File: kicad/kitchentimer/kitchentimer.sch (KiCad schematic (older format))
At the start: 34 parts, among them J1 CONN_01X06, SW1 SWITCH, SW2 SWITCH, SW3 SWITCH, SW4 SWITCH, SW5 SWITCH, SW6 SWITCH, SW7 SWITCH, U1 74HC595, U2 74HC595, U3 74LS165, U4 74HC595, U5 74HC595

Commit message: Associate components
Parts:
- AFF1, AFF2: footprint (none) -> Displays_7-Segment:7SegmentLED_LTS6760_LTS6780
- D1, D2, D3, D4, D5, D6: footprint (none) -> LEDs:LED_0805
- J1: footprint (none) -> Pin_Headers:Pin_Header_Straight_1x06
- R1, R10, R11, R12, R13, R2, R3, R4, R5, R6, R7, R8, R9: footprint (none) -> Resistors_SMD:R_0805_HandSoldering
- SW1, SW2, SW3, SW4, SW5, SW6, SW7: footprint (none) -> Buttons_Switches_THT:SW_PUSH_6mm
- U1, U2, U3, U4, U5: footprint (none) -> Housings_DIP:DIP-16_W7.62mm
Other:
- note added: "LATCH SWITCH"
- note removed: "LATCH 165"
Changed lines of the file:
@@
 F 0 "U5" V 8850 1000 50  0000 L CNN
 F 1 "74HC595" V 8850 1500 50  0000 L CNN
-F 2 "" H 3850 -1800 50  0001 C CNN
+F 2 "Housings_DIP:DIP-16_W7.62mm" H 3850 -1800 50  0001 C CNN
 F 3 "" H 3850 -1800 50  0001 C CNN
 	1    8850 1700
@@
 F 0 "U4" V 8750 2900 50  0000 L CNN
 F 1 "74HC595" V 8750 3400 50  0000 L CNN
-F 2 "" H 3750 100 50  0001 C CNN
+F 2 "Housings_DIP:DIP-16_W7.62mm" H 3750 100 50  0001 C CNN
 F 3 "" H 3750 100 50  0001 C CNN
 	1    8750 3600
@@
 F 0 "U1" V 3800 3700 50  0000 L CNN
 F 1 "74HC595" V 3800 4200 50  0000 L CNN
-F 2 "" H -1200 900 50  0001 C CNN
+F 2 "Housings_DIP:DIP-16_W7.62mm" H -1200 900 50  0001 C CNN
 F 3 "" H -1200 900 50  0001 C CNN
 	1    3800 4400
@@
 F 0 "U2" V 5700 1900 50  0000 L CNN
 F 1 "74HC595" V 5700 2450 50  0000 L CNN
-F 2 "" H 700 -850 50  0001 C CNN
+F 2 "Housings_DIP:DIP-16_W7.62mm" H 700 -850 50  0001 C CNN
 F 3 "" H 700 -850 50  0001 C CNN
 	1    5700 2650
@@
 F 0 "J1" V 5015 762 50  0000 R CNN
 F 1 "CONN_01X06" V 4924 762 50  0000 R CNN
-F 2 "" H -200 0   50  0001 C CNN
+F 2 "Pin_Headers:Pin_Header_Straight_1x06" H -200 0   50  0001 C CNN
 F 3 "" H -200 0   50  0001 C CNN
 	1    5050 1100
@@
 F 0 "U3" V 5800 5250 50  0000 R CNN
 F 1 "74LS165" V 5800 4600 50  0000 R CNN
-F 2 "" H 2750 3050 50  0001 C CNN
+F 2 "Housings_DIP:DIP-16_W7.62mm" H 2750 3050 50  0001 C CNN
 F 3 "" H 2750 3050 50  0001 C CNN
 	1    5800 4450
@@
 NoConn ~ 5200 5150
 NoConn ~ 5400 3750
-Text Notes 6700 4000 3    60   ~ 0
-LATCH 165
+Text Notes 6650 4550 1    60   ~ 0
+LATCH SWITCH
 $Comp
 L 7SEGMENTS AFF1
@@
 F 0 "AFF1" H 10500 2425 50  0000 C CNN
 F 1 "7SEGMENTS" H 10500 2334 50  0000 C CNN
-F 2 "" H 3350 -2800 50  0001 C CNN
+F 2 "Displays_7-Segment:7SegmentLED_LTS6760_LTS6780" H 3350 -2800 50  0001 C CNN
 F 3 "" H 3350 -2800 50  0001 C CNN
 	1    10500 1750
@@
 F 0 "AFF2" H 10550 4575 50  0000 C CNN
 F 1 "7SEGMENTS" H 10550 4484 50  0000 C CNN
-F 2 "" H 3400 -650 50  0001 C CNN
+F 2 "Displays_7-Segment:7SegmentLED_LTS6760_LTS6780" H 3400 -650 50  0001 C CNN
 F 3 "" H 3400 -650 50  0001 C CNN
 	1    10550 3900
@@
 F 0 "D6" V 2488 5933 50  0000 R CNN
 F 1 "LED" V 2397 5933 50  0000 R CNN
-F 2 "" H -1000 600 50  0001 C CNN
+F 2 "LEDs:LED_0805" H -1000 600 50  0001 C CNN
 F 3 "" H -1000 600 50  0001 C CNN
 	1    2450 6050
@@
 F 0 "R6" H 2380 5604 50  0000 R CNN
 F 1 "R" H 2380 5695 50  0000 R CNN
-F 2 "" V -920 0   50  0001 C CNN
+F 2 "Resistors_SMD:R_0805_HandSoldering" V -920 0   50  0001 C CNN
 F 3 "" H -850 0   50  0001 C CNN
 	1    2450 5650
@@
 F 0 "R5" H 2230 5604 50  0000 R CNN
 F 1 "R" H 2230 5695 50  0000 R CNN
-F 2 "" V -1070 0   50  0001 C CNN
+F 2 "Resistors_SMD:R_0805_HandSoldering" V -1070 0   50  0001 C CNN
 F 3 "" H -1000 0   50  0001 C CNN
 	1    2300 5650
@@
 F 0 "D5" V 2338 5933 50  0000 R CNN
 F 1 "LED" V 2247 5933 50  0000 R CNN
-F 2 "" H -1150 600 50  0001 C CNN
+F 2 "LEDs:LED_0805" H -1150 600 50  0001 C CNN
 F 3 "" H -1150 600 50  0001 C CNN
 	1    2300 6050
@@
 F 0 "R4" H 2080 5604 50  0000 R CNN
 F 1 "R" H 2080 5695 50  0000 R CNN
-F 2 "" V -1220 0   50  0001 C CNN
+F 2 "Resistors_SMD:R_0805_HandSoldering" V -1220 0   50  0001 C CNN
 F 3 "" H -1150 0   50  0001 C CNN
 	1    2150 5650
@@
 F 0 "D4" V 2188 5933 50  0000 R CNN
 F 1 "LED" V 2097 5933 50  0000 R CNN
-F 2 "" H -1300 600 50  0001 C CNN
+F 2 "LEDs:LED_0805" H -1300 600 50  0001 C CNN
 F 3 "" H -1300 600 50  0001 C CNN
 	1    2150 6050
@@
 F 0 "R3" H 1930 5604 50  0000 R CNN
 F 1 "R" H 1930 5695 50  0000 R CNN
-F 2 "" V -1370 0   50  0001 C CNN
+F 2 "Resistors_SMD:R_0805_HandSoldering" V -1370 0   50  0001 C CNN
 F 3 "" H -1300 0   50  0001 C CNN
 	1    2000 5650
@@
 F 0 "D3" V 2038 5933 50  0000 R CNN
 F 1 "LED" V 1947 5933 50  0000 R CNN
-F 2 "" H -1450 600 50  0001 C CNN
+F 2 "LEDs:LED_0805" H -1450 600 50  0001 C CNN
 F 3 "" H -1450 600 50  0001 C CNN
 	1    2000 6050
@@
 F 0 "D2" V 1888 5933 50  0000 R CNN
 F 1 "LED" V 1797 5933 50  0000 R CNN
-F 2 "" H -1600 600 50  0001 C CNN
+F 2 "LEDs:LED_0805" H -1600 600 50  0001 C CNN
 F 3 "" H -1600 600 50  0001 C CNN
 	1    1850 6050
@@
 F 0 "D1" V 1738 5933 50  0000 R CNN
 F 1 "LED" V 1647 5933 50  0000 R CNN
-F 2 "" H -1750 600 50  0001 C CNN
+F 2 "LEDs:LED_0805" H -1750 600 50  0001 C CNN
 F 3 "" H -1750 600 50  0001 C CNN
 	1    1700 6050
@@
 F 0 "R2" H 1780 5604 50  0000 R CNN
 F 1 "R" H 1780 5695 50  0000 R CNN
-F 2 "" V -1520 0   50  0001 C CNN
+F 2 "Resistors_SMD:R_0805_HandSoldering" V -1520 0   50  0001 C CNN
 F 3 "" H -1450 0   50  0001 C CNN
 	1    1850 5650
@@
 F 0 "R1" H 1630 5604 50  0000 R CNN
 F 1 "R" H 1630 5695 50  0000 R CNN
-F 2 "" V -1670 0   50  0001 C CNN
+F 2 "Resistors_SMD:R_0805_HandSoldering" V -1670 0   50  0001 C CNN
 F 3 "" H -1600 0   50  0001 C CNN
 	1    1700 5650
@@
 F 0 "SW1" V 4650 5850 60  0000 L CNN
 F 1 "SWITCH" H 5250 5900 60  0000 L CNN
-F 2 "" H 1550 3450 60  0000 C CNN
+F 2 "Buttons_Switches_THT:SW_PUSH_6mm" H 1550 3450 60  0001 C CNN
 F 3 "" H 1550 3450 60  0000 C CNN
 	1    4950 5900
@@
 F 0 "R7" H 5020 6696 50  0000 L CNN
 F 1 "R" H 5020 6605 50  0000 L CNN
-F 2 "" V 230 700 50  0001 C CNN
+F 2 "Resistors_SMD:R_0805_HandSoldering" V 230 700 50  0001 C CNN
 F 3 "" H 300 700 50  0001 C CNN
 	1    4950 6650
@@
 F 0 "R8" H 5170 6696 50  0000 L CNN
 F 1 "R" H 5170 6605 50  0000 L CNN
-F 2 "" V 380 700 50  0001 C CNN
+F 2 "Resistors_SMD:R_0805_HandSoldering" V 380 700 50  0001 C CNN
 F 3 "" H 450 700 50  0001 C CNN
 	1    5100 6650
@@
 F 0 "SW2" V 4800 5850 60  0000 L CNN
 F 1 "SWITCH" H 5400 5900 60  0000 L CNN
-F 2 "" H 1700 3450 60  0000 C CNN
+F 2 "Buttons_Switches_THT:SW_PUSH_6mm" H 1700 3450 60  0001 C CNN
 F 3 "" H 1700 3450 60  0000 C CNN
 	1    5100 5900
@@
 F 0 "SW3" V 4950 5850 60  0000 L CNN
 F 1 "SWITCH" H 5550 5900 60  0000 L CNN
-F 2 "" H 1850 3450 60  0000 C CNN
+F 2 "Buttons_Switches_THT:SW_PUSH_6mm" H 1850 3450 60  0001 C CNN
 F 3 "" H 1850 3450 60  0000 C CNN
 	1    5250 5900
@@
 F 0 "R9" H 5320 6696 50  0000 L CNN
 F 1 "R" H 5320 6605 50  0000 L CNN
-F 2 "" V 530 700 50  0001 C CNN
+F 2 "Resistors_SMD:R_0805_HandSoldering" V 530 700 50  0001 C CNN
 F 3 "" H 600 700 50  0001 C CNN
 	1    5250 6650
@@
 F 0 "R10" H 5470 6696 50  0000 L CNN
 F 1 "R" H 5470 6605 50  0000 L CNN
-F 2 "" V 680 700 50  0001 C CNN
+F 2 "Resistors_SMD:R_0805_HandSoldering" V 680 700 50  0001 C CNN
 F 3 "" H 750 700 50  0001 C CNN
 	1    5400 6650
@@
 F 0 "R11" H 5620 6696 50  0000 L CNN
 F 1 "R" H 5620 6605 50  0000 L CNN
-F 2 "" V 830 700 50  0001 C CNN
+F 2 "Resistors_SMD:R_0805_HandSoldering" V 830 700 50  0001 C CNN
 F 3 "" H 900 700 50  0001 C CNN
 	1    5550 6650
@@
 F 0 "R12" H 5770 6696 50  0000 L CNN
 F 1 "R" H 5770 6605 50  0000 L CNN
-F 2 "" V 980 700 50  0001 C CNN
+F 2 "Resistors_SMD:R_0805_HandSoldering" V 980 700 50  0001 C CNN
 F 3 "" H 1050 700 50  0001 C CNN
 	1    5700 6650
@@
 F 0 "R13" H 5920 6696 50  0000 L CNN
 F 1 "R" H 5920 6605 50  0000 L CNN
-F 2 "" V 1130 700 50  0001 C CNN
+F 2 "Resistors_SMD:R_0805_HandSoldering" V 1130 700 50  0001 C CNN
 F 3 "" H 1200 700 50  0001 C CNN
 	1    5850 6650
@@
 F 0 "SW4" V 5100 5850 60  0000 L CNN
 F 1 "SWITCH" H 5700 5900 60  0000 L CNN
-F 2 "" H 2000 3450 60  0000 C CNN
+F 2 "Buttons_Switches_THT:SW_PUSH_6mm" H 2000 3450 60  0001 C CNN
 F 3 "" H 2000 3450 60  0000 C CNN
 	1    5400 5900
@@
 F 0 "SW5" V 5250 5850 60  0000 L CNN
 F 1 "SWITCH" H 5850 5900 60  0000 L CNN
-F 2 "" H 2150 3450 60  0000 C CNN
+F 2 "Buttons_Switches_THT:SW_PUSH_6mm" H 2150 3450 60  0001 C CNN
 F 3 "" H 2150 3450 60  0000 C CNN
 	1    5550 5900
@@
 F 0 "SW6" V 5400 5850 60  0000 L CNN
 F 1 "SWITCH" H 6000 5900 60  0000 L CNN
-F 2 "" H 2300 3450 60  0000 C CNN
+F 2 "Buttons_Switches_THT:SW_PUSH_6mm" H 2300 3450 60  0001 C CNN
 F 3 "" H 2300 3450 60  0000 C CNN
 	1    5700 5900
@@
 F 0 "SW7" V 5550 5850 60  0000 L CNN
 F 1 "SWITCH" H 6150 5900 60  0000 L CNN
-F 2 "" H 2450 3450 60  0000 C CNN
+F 2 "Buttons_Switches_THT:SW_PUSH_6mm" H 2450 3450 60  0001 C CNN
 F 3 "" H 2450 3450 60  0000 C CNN
 	1    5850 5900

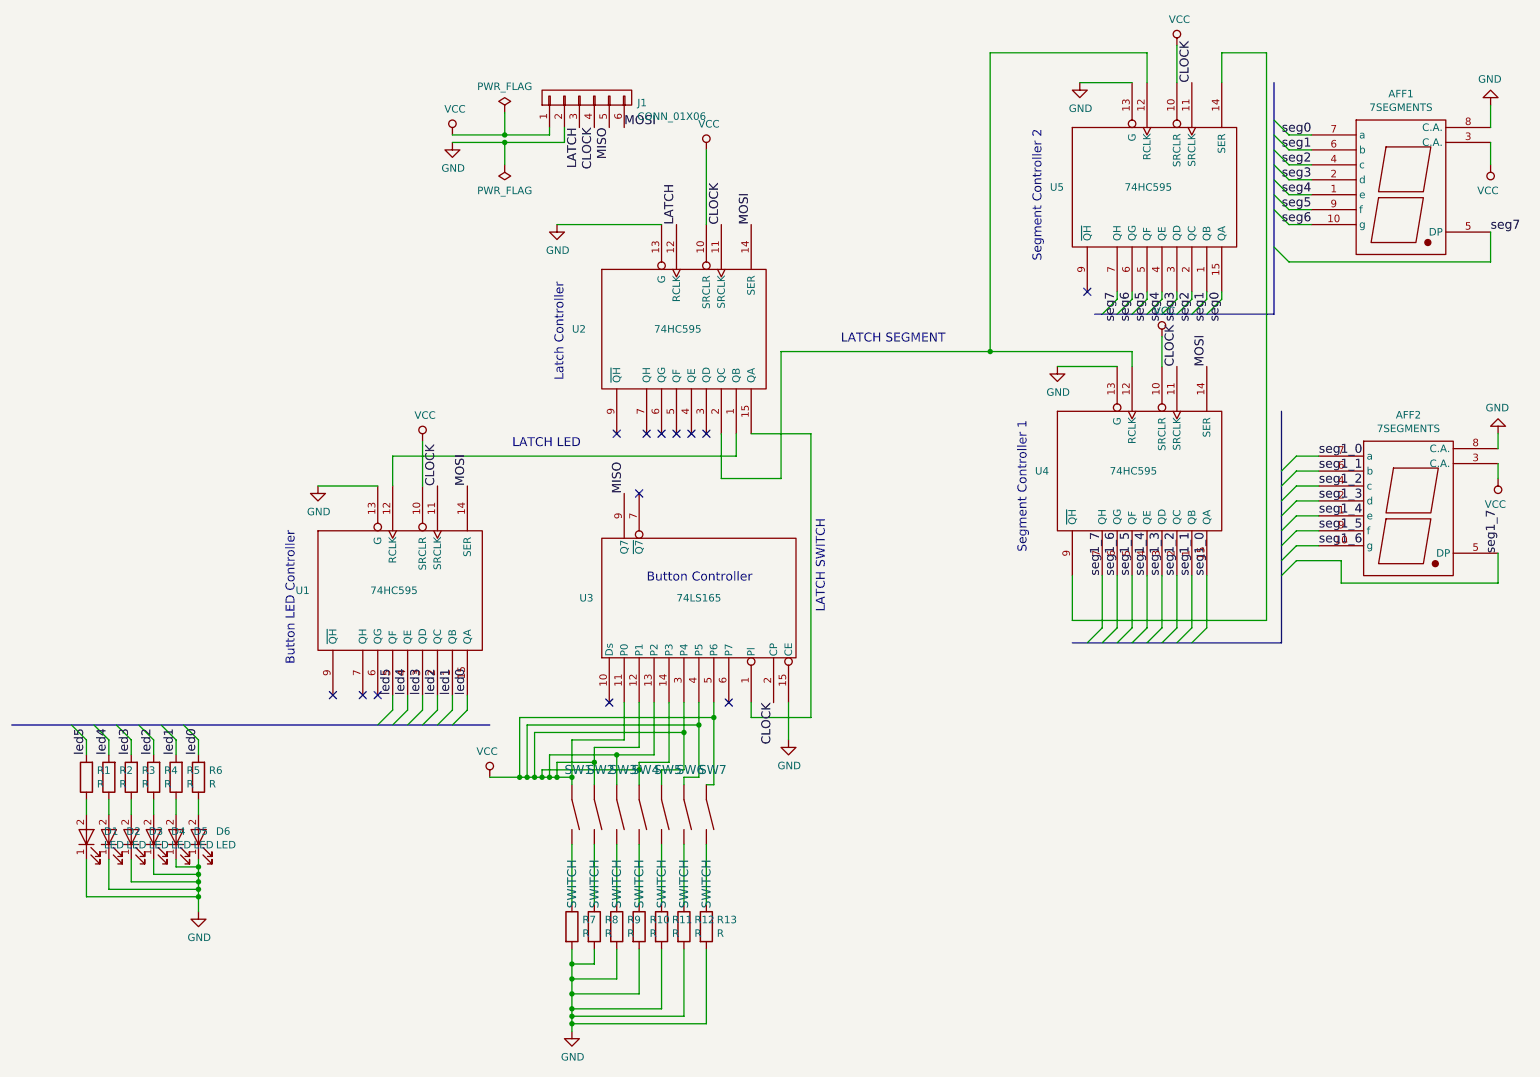
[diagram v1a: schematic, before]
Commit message: fix the switch circuit.
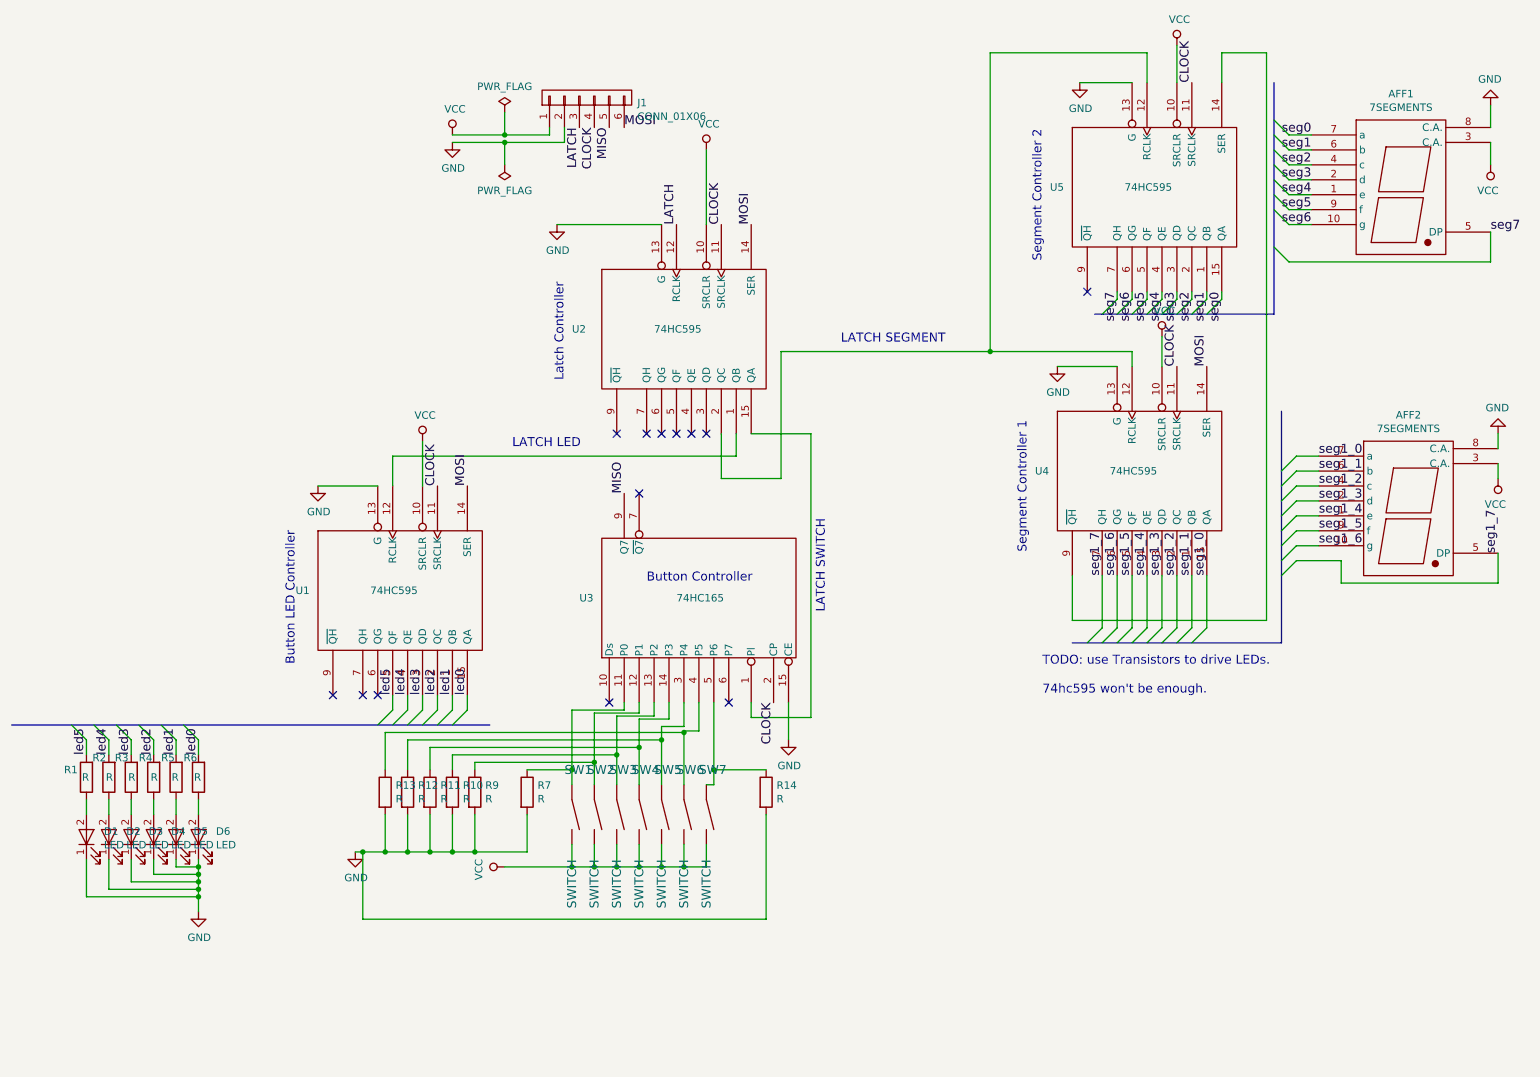
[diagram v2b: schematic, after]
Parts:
- removed R8: R, Resistors_SMD:R_0805_HandSoldering, symbol R
- added R14: R, Resistors_SMD:R_0805_HandSoldering, symbol R
- U3: value 74LS165 -> 74HC165
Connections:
- net GND: now also R14.2
- net VCC: now also SW1.2, SW2.2, SW3.2, SW4.2, SW5.2, SW6.2, SW7.2; no longer SW1.1, SW2.1, SW3.1, SW4.1, SW5.1, SW6.1, SW7.1, U3.11 (P0), U3.12 (P1), U3.13 (P2), U3.14 (P3), U3.3 (P4), U3.4 (P5), U3.5 (P6)
- net at R7.1: now also SW1.1, U3.11 (P0); no longer SW1.2
- net at R9.1: now also SW2.1, U3.12 (P1); no longer SW3.2
- net at R10.1: now also SW3.1, U3.13 (P2); no longer SW4.2
- net at R11.1: now also SW4.1, U3.14 (P3); no longer SW5.2
- net at R12.1: now also SW5.1, U3.3 (P4); no longer SW6.2
- net at R13.1: now also SW6.1, U3.4 (P5); no longer SW7.2
- new net: R14.1, SW7.1, U3.5 (P6)
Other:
- note added: "TODO: use Transistors to drive LEDs.\n\n74hc595 won't be enough.\n"
- moved on the sheet: R10, R11, R12, R13, R7, R9

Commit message: fix circuit for 7 segment display.
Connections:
- net GND: no longer AFF1.8 (C.A.), AFF2.8 (C.A.)
- no-connect marks 13 -> 15
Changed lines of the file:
@@
-$EndComp
-$Comp
-L GND #PWR017
-U 1 1 5893BB10
-P 11100 1150
-F 0 "#PWR017" H 6600 -450 50  0001 C CNN
-F 1 "GND" H 11105 977 50  0000 C CNN
-F 2 "" H 6600 -200 50  0001 C CNN
-F 3 "" H 6600 -200 50  0001 C CNN
-	1    11100 1150
-	-1   0    0    1
-$EndComp
-$Comp
-L GND #PWR018
-U 1 1 5893BC1C
-P 11150 3350
-F 0 "#PWR018" H 6650 1750 50  0001 C CNN
-F 1 "GND" H 11155 3177 50  0000 C CNN
-F 2 "" H 6650 2000 50  0001 C CNN
-F 3 "" H 6650 2000 50  0001 C CNN
-	1    11150 3350
-	-1   0    0    1
 $EndComp
 $Comp
@@
 	11100 1400 11100 1550
 Wire Wire Line
-	11100 1150 11100 1300
-Wire Wire Line
-	11150 3350 11150 3450
-Wire Wire Line
 	5300 5150 5300 5200
 Wire Wire Line
@@
 Text Notes 8100 5100 0    60   ~ 0
 TODO: use Transistors to drive LEDs.\n\n74hc595 won't be enough.\n
+NoConn ~ 11150 3450
+NoConn ~ 11100 1300
 $EndSCHEMATC
